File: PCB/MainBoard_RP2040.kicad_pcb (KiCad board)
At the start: 2 copper layers, 259.5 x 132.8 mm, 61 parts, among them J1 USB4105-GF-A, U1 ADC108S022CIMTX/NOPB, U10 DRV5053VAQDBZR, U11 DRV5053VAQDBZR, U12 DRV5053VAQDBZR, U13 DRV5053VAQDBZR, U14 DRV5053VAQDBZR, U15 DRV5053VAQDBZR, U16 DRV5053VAQDBZR, U17 DRV5053VAQDBZR, U18 DRV5053VAQDBZR, U19 DRV5053VAQDBZR, U20 ATmega32U4-A, U3 ADC108S022CIMTX/NOPB, U37 Pico, U4 DRV5053VAQDBZR, U5 DRV5053VAQDBZR, U6 DRV5053VAQDBZR, U7 DRV5053VAQDBZR, U8 DRV5053VAQDBZR, U9 DRV5053VAQDBZR, Y2 Crystal_GND24

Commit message: Removed other controller boards from RP2040
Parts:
- removed Brooks1: ~, BrooksBoards:BrooksP5Plus
- removed U36: ~, BrooksBoards:BrooksP5Mini
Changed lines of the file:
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@@
-		)
-	)
-	(footprint "BrooksBoards:BrooksP5Plus"
-		(layer "F.Cu")
-		(at 228.5 125 180)
-		(property "Reference" "Brooks1"
-			(at 0 -0.5 180)
-			(unlocked yes)
-			(layer "F.SilkS")
-			(effects
-				(font
-					(size 1 1)
-					(thickness 0.1)
-				)
-			)
-		)
-		(property "Value" "~"
-			(at 0 1 180)
-			(unlocked yes)
-			(layer "F.Fab")
-			(effects
-				(font
-					(size 1 1)
-					(thickness 0.15)
-				)
-			)
-		)
-		(property "Footprint" "BrooksBoards:BrooksP5Plus"
-			(at 0 0 180)
-			(unlocked yes)
-			(layer "F.Fab")
-			(hide yes)
-			(effects
-				(font
-					(size 1 1)
-					(thickness 0.15)
-				)
-			)
-		)
-		(property "Datasheet" ""
-			(at 0 0 180)
-			(unlocked yes)
-			(layer "F.Fab")
-			(hide yes)
-			(effects
-				(font
-					(size 1 1)
-					(thickness 0.15)
-				)
-			)
-		)
-		(property "Description" ""
-			(at 0 0 180)
-			(unlocked yes)
-			(layer "F.Fab")
-			(hide yes)
-			(effects
-				(font
-					(size 1 1)
-					(thickness 0.15)
-				)
-			)
-		)
-		(sheetname "Root")
-		(sheetfile "MainBoard.kicad_sch")
-		(attr through_hole)
-		(fp_rect
-			(start -48.2 -22.6)
-			(end 47.9 22.5)
-			(stroke
-				(width 0.1)
-				(type default)
-			)
-			(fill none)
-			(layer "F.SilkS")
-		)
-		(fp_text user "${REFERENCE}"
-			(at 0 2.5 180)
-			(unlocked yes)
-			(layer "F.Fab")
-			(effects
-				(font
-					(size 1 1)
-					(thickness 0.15)
-				)
-			)
 		)
 	)
@@
 				)
 			)
-		)
-	)
-	(footprint "BrooksBoards:BrooksP5Mini"
-		(layer "F.Cu")
-		(at 215.5 123.5)
-		(property "Reference" "U36"
-			(at 0 -0.5 0)
-			(unlocked yes)
-			(layer "F.SilkS")
-			(effects
-				(font
-					(size 1 1)
-					(thickness 0.1)
-				)
-			)
-		)
-		(property "Value" "~"
-			(at 0 1 0)
-			(unlocked yes)
-			(layer "F.Fab")
-			(effects
-				(font
-					(size 1 1)
-					(thickness 0.15)
-				)
-			)
-		)
-		(property "Footprint" "BrooksBoards:BrooksP5Mini"
-			(at 0 0 0)
-			(unlocked yes)
-			(layer "F.Fab")
-			(hide yes)
-			(effects
-				(font
-					(size 1 1)
-					(thickness 0.15)
-				)
-			)
-		)
-		(property "Datasheet" ""
-			(at 0 0 0)
-			(unlocked yes)
-			(layer "F.Fab")
-			(hide yes)
-			(effects
-				(font
-					(size 1 1)
-					(thickness 0.15)
-				)
-			)
-		)
-		(property "Description" ""
-			(at 0 0 0)
-			(unlocked yes)
-			(layer "F.Fab")
-			(hide yes)
-			(effects
-				(font
-					(size 1 1)
-					(thickness 0.15)
-				)
-			)
-		)
-		(sheetname "Root")
-		(sheetfile "MainBoard.kicad_sch")
-		(attr through_hole)
-		(fp_rect
-			(start -20 -20)
-			(end 20 20)
-			(stroke
-				(width 0.1)
-				(type default)
-			)
-			(fill none)
-			(layer "F.SilkS")
-		)
-		(fp_text user "${REFERENCE}"
-			(at 0 2.5 0)
-			(unlocked yes)
-			(layer "F.Fab")
-			(effects
-				(font
-					(size 1 1)
-					(thickness 0.15)
-				)
-			)

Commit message: Confirmed working, moving towards PCB v1.1
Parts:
- removed D1: LED_GREEN, LED_SMD:LED_0201_0603Metric
- removed R4: 1k, Resistor_SMD:R_0603_1608Metric
- added J2: Conn_01x06_Pin, Connector_PinHeader_2.54mm:PinHeader_2x03_P2.54mm_Vertical, F.Cu at (52.0, 71.5)
- added MB1: MagicBoots, Mayflash:MagicBoots, F.Cu at (175.0, 127.5)
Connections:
- net Net-(U20-~{RESET}) renamed /RST
- U37 pad 24: unconnected-(U37-GPIO18-Pad24) -> /HOST_D-
- U37 pad 25: unconnected-(U37-GPIO19-Pad25) -> /HOST_D+
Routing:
- net /HOST_D-: track 0.00 -> 148.7 mm
- net /HOST_D+: track 0.00 -> 143.7 mm
- net VCC: track 359.8 -> 454.2 mm, vias 6 -> 7
- net MOSI: track 153.0 -> 200.9 mm
- net MISO: track 152.7 -> 184.0 mm, vias 3 -> 4
- net SCLK: track 156.1 -> 173.6 mm, vias 3 -> 6
- net /RST: track 14.9 -> 25.8 mm
- net GND: track 109.8 -> 112.5 mm, vias 148 -> 191
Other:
- board size 259.5 x 132.8 mm -> 259.5 x 133 mm
- board text added: "Tristan Melton FaradayFightstick v1.1"
- board text removed: "MeltonTech"

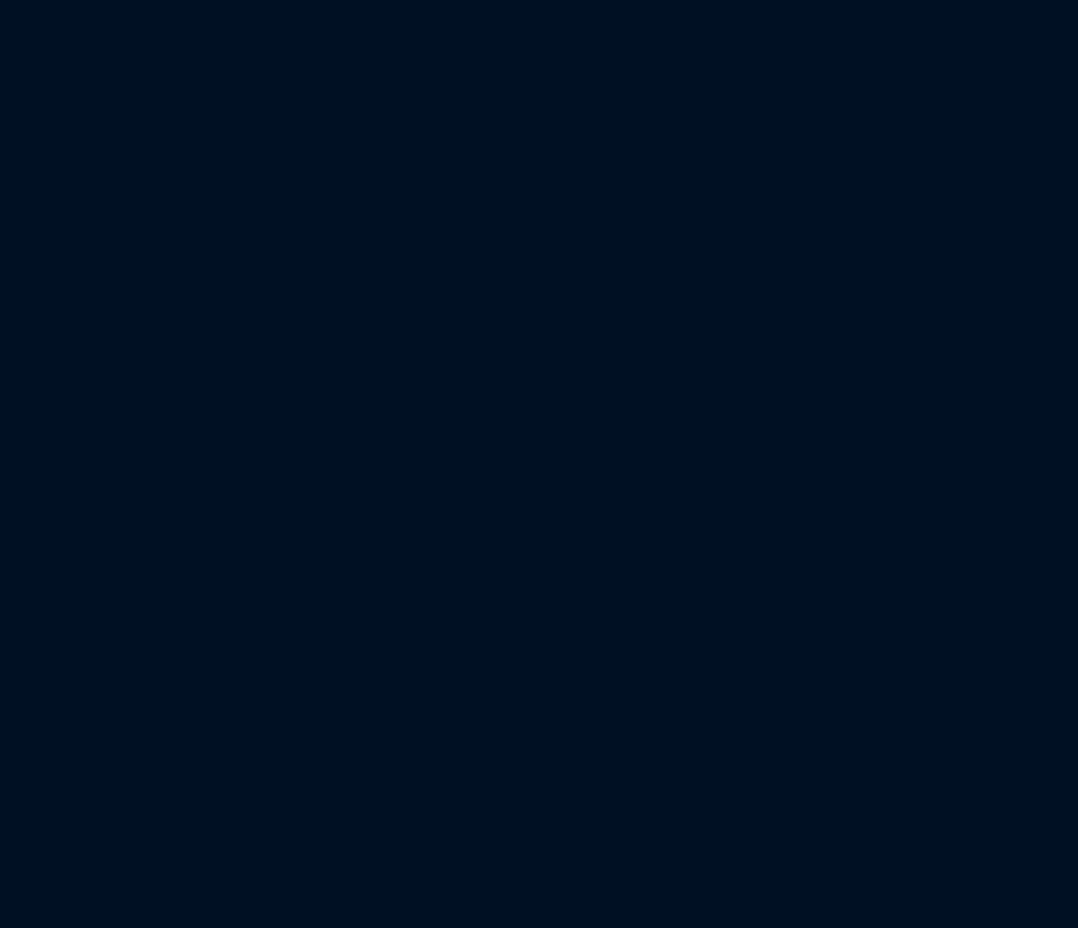
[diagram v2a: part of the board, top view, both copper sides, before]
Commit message: Added the additional components to support the ADCs
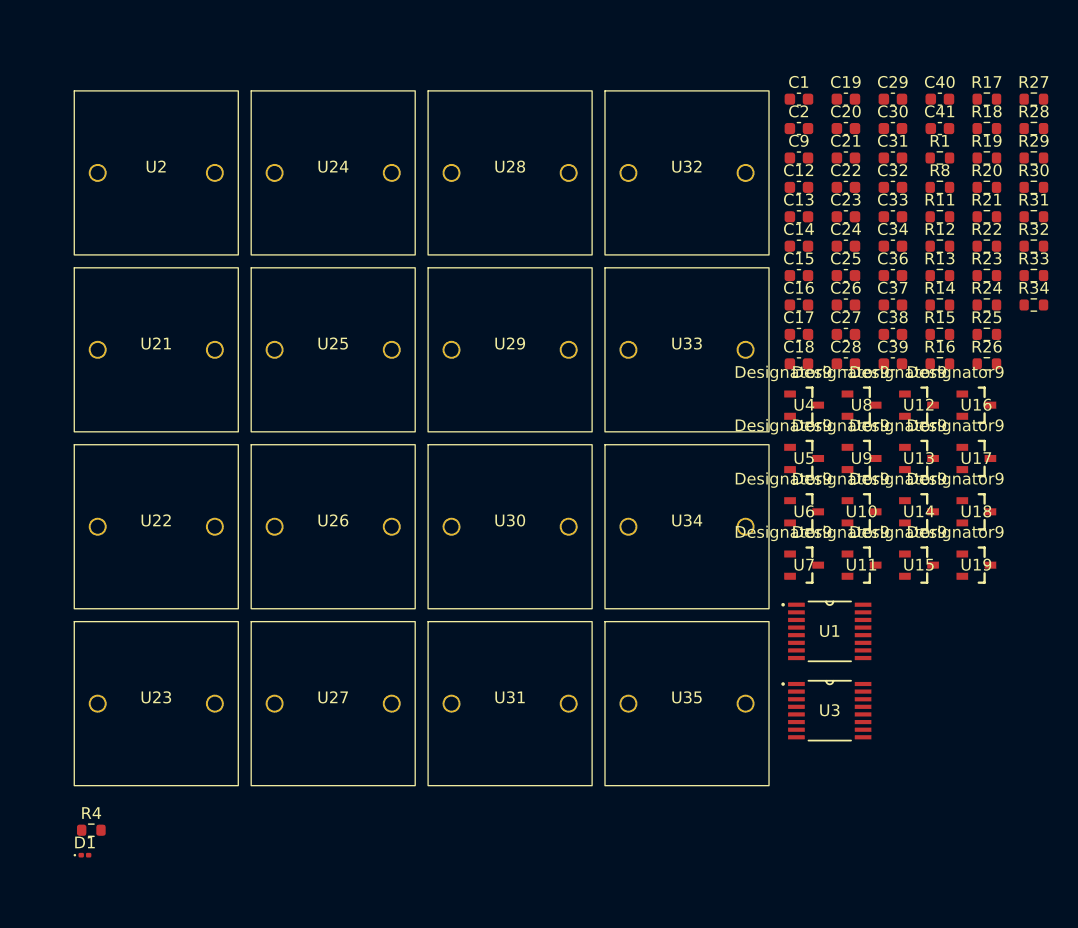
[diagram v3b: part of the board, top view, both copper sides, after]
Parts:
- added C1: 0.1u, Capacitor_SMD:C_0603_1608Metric, F.Cu at (384.0, 30.0)
- added C12: 1u, Capacitor_SMD:C_0603_1608Metric, F.Cu at (384.0, 37.6)
- added C13: 1n, Capacitor_SMD:C_0603_1608Metric, F.Cu at (384.0, 40.1)
- added C14: 1n, Capacitor_SMD:C_0603_1608Metric, F.Cu at (384.0, 42.6)
- added C15: 1n, Capacitor_SMD:C_0603_1608Metric, F.Cu at (384.0, 45.1)
- added C16: 1n, Capacitor_SMD:C_0603_1608Metric, F.Cu at (384.0, 47.6)
- added C17: 1n, Capacitor_SMD:C_0603_1608Metric, F.Cu at (384.0, 50.1)
- added C18: 1n, Capacitor_SMD:C_0603_1608Metric, F.Cu at (384.0, 52.6)
- added C19: 0.1u, Capacitor_SMD:C_0603_1608Metric, F.Cu at (388.0, 30.0)
- added C2: 1u, Capacitor_SMD:C_0603_1608Metric, F.Cu at (384.0, 32.5)
- added C20: 1u, Capacitor_SMD:C_0603_1608Metric, F.Cu at (388.0, 32.5)
- added C21: 1n, Capacitor_SMD:C_0603_1608Metric, F.Cu at (388.0, 35.1)
- added C22: 1n, Capacitor_SMD:C_0603_1608Metric, F.Cu at (388.0, 37.6)
- added C23: 1n, Capacitor_SMD:C_0603_1608Metric, F.Cu at (388.0, 40.1)
- added C24: 1n, Capacitor_SMD:C_0603_1608Metric, F.Cu at (388.0, 42.6)
- added C25: 1n, Capacitor_SMD:C_0603_1608Metric, F.Cu at (388.0, 45.1)
- added C26: 1n, Capacitor_SMD:C_0603_1608Metric, F.Cu at (388.0, 47.6)
- added C27: 1n, Capacitor_SMD:C_0603_1608Metric, F.Cu at (388.0, 50.1)
- added C28: 1n, Capacitor_SMD:C_0603_1608Metric, F.Cu at (388.0, 52.6)
- added C29: 1n, Capacitor_SMD:C_0603_1608Metric, F.Cu at (392.0, 30.0)
- added C30: 1n, Capacitor_SMD:C_0603_1608Metric, F.Cu at (392.0, 32.5)
- added C31: 1n, Capacitor_SMD:C_0603_1608Metric, F.Cu at (392.0, 35.1)
- added C32: 1n, Capacitor_SMD:C_0603_1608Metric, F.Cu at (392.0, 37.6)
- added C33: 0.1u, Capacitor_SMD:C_0603_1608Metric, F.Cu at (392.0, 40.1)
- added C34: 1u, Capacitor_SMD:C_0603_1608Metric, F.Cu at (392.0, 42.6)
- added C36: 1n, Capacitor_SMD:C_0603_1608Metric, F.Cu at (392.0, 45.1)
- added C37: 1n, Capacitor_SMD:C_0603_1608Metric, F.Cu at (392.0, 47.6)
- added C38: 1n, Capacitor_SMD:C_0603_1608Metric, F.Cu at (392.0, 50.1)
- added C39: 1n, Capacitor_SMD:C_0603_1608Metric, F.Cu at (392.0, 52.6)
- added C40: 1n, Capacitor_SMD:C_0603_1608Metric, F.Cu at (396.1, 30.0)
- added C41: 1n, Capacitor_SMD:C_0603_1608Metric, F.Cu at (396.1, 32.5)
- added C9: 0.1u, Capacitor_SMD:C_0603_1608Metric, F.Cu at (384.0, 35.1)
- added D1: LED_GREEN, LED_SMD:LED_0201_0603Metric, F.Cu at (323.1, 94.6)
- added R1: 22, Resistor_SMD:R_0603_1608Metric, F.Cu at (396.1, 35.1)
- added R11: 22, Resistor_SMD:R_0603_1608Metric, F.Cu at (396.1, 40.1)
- added R12: 22, Resistor_SMD:R_0603_1608Metric, F.Cu at (396.1, 42.6)
- added R13: 22, Resistor_SMD:R_0603_1608Metric, F.Cu at (396.1, 45.1)
- added R14: 22, Resistor_SMD:R_0603_1608Metric, F.Cu at (396.1, 47.6)
- added R15: 22, Resistor_SMD:R_0603_1608Metric, F.Cu at (396.1, 50.1)
- added R16: 22, Resistor_SMD:R_0603_1608Metric, F.Cu at (396.1, 52.6)
- added R17: 22, Resistor_SMD:R_0603_1608Metric, F.Cu at (400.1, 30.0)
- added R18: 22, Resistor_SMD:R_0603_1608Metric, F.Cu at (400.1, 32.5)
- added R19: 22, Resistor_SMD:R_0603_1608Metric, F.Cu at (400.1, 35.1)
- added R20: 22, Resistor_SMD:R_0603_1608Metric, F.Cu at (400.1, 37.6)
- added R21: 22, Resistor_SMD:R_0603_1608Metric, F.Cu at (400.1, 40.1)
- added R22: 22, Resistor_SMD:R_0603_1608Metric, F.Cu at (400.1, 42.6)
- added R23: 22, Resistor_SMD:R_0603_1608Metric, F.Cu at (400.1, 45.1)
- added R24: 22, Resistor_SMD:R_0603_1608Metric, F.Cu at (400.1, 47.6)
- added R25: 22, Resistor_SMD:R_0603_1608Metric, F.Cu at (400.1, 50.1)
- added R26: 22, Resistor_SMD:R_0603_1608Metric, F.Cu at (400.1, 52.6)
- added R27: 51, Resistor_SMD:R_0603_1608Metric, F.Cu at (404.1, 30.0)
- added R28: 22, Resistor_SMD:R_0603_1608Metric, F.Cu at (404.1, 32.5)
- added R29: 22, Resistor_SMD:R_0603_1608Metric, F.Cu at (404.1, 35.1)
- added R30: 22, Resistor_SMD:R_0603_1608Metric, F.Cu at (404.1, 37.6)
- added R31: 22, Resistor_SMD:R_0603_1608Metric, F.Cu at (404.1, 40.1)
- added R32: 22, Resistor_SMD:R_0603_1608Metric, F.Cu at (404.1, 42.6)
- added R33: 22, Resistor_SMD:R_0603_1608Metric, F.Cu at (404.1, 45.1)
- added R34: 51, Resistor_SMD:R_0603_1608Metric, F.Cu at (404.1, 47.6)
- added R4: 1k, Resistor_SMD:R_0603_1608Metric, F.Cu at (323.6, 92.4)
- added R8: 22, Resistor_SMD:R_0603_1608Metric, F.Cu at (396.1, 37.6)
- added U1: ADC108S022CIMTX/NOPB, ADCs:MTC16, F.Cu at (386.7, 75.5)
- added U10: DRV5053VAQDBZR, HallEffect:DBZ0003A_N, F.Cu at (389.4, 65.3)
- added U11: DRV5053VAQDBZR, HallEffect:DBZ0003A_N, F.Cu at (389.4, 69.8)
- added U12: DRV5053VAQDBZR, HallEffect:DBZ0003A_N, F.Cu at (394.3, 56.2)
- added U13: DRV5053VAQDBZR, HallEffect:DBZ0003A_N, F.Cu at (394.3, 60.7)
- added U14: DRV5053VAQDBZR, HallEffect:DBZ0003A_N, F.Cu at (394.3, 65.3)
- added U15: DRV5053VAQDBZR, HallEffect:DBZ0003A_N, F.Cu at (394.3, 69.8)
- added U16: DRV5053VAQDBZR, HallEffect:DBZ0003A_N, F.Cu at (399.2, 56.2)
- added U17: DRV5053VAQDBZR, HallEffect:DBZ0003A_N, F.Cu at (399.2, 60.7)
- added U18: DRV5053VAQDBZR, HallEffect:DBZ0003A_N, F.Cu at (399.2, 65.3)
- added U19: DRV5053VAQDBZR, HallEffect:DBZ0003A_N, F.Cu at (399.2, 69.8)
- added U2: ~, key-switches:Gateron Jade Pro Magnetic, F.Cu at (329.2, 36.3)
- added U21: ~, key-switches:Gateron Jade Pro Magnetic, F.Cu at (329.2, 51.4)
- added U22: ~, key-switches:Gateron Jade Pro Magnetic, F.Cu at (329.2, 66.5)
- added U23: ~, key-switches:Gateron Jade Pro Magnetic, F.Cu at (329.2, 81.6)
- added U24: ~, key-switches:Gateron Jade Pro Magnetic, F.Cu at (344.3, 36.3)
- added U25: ~, key-switches:Gateron Jade Pro Magnetic, F.Cu at (344.3, 51.4)
- added U26: ~, key-switches:Gateron Jade Pro Magnetic, F.Cu at (344.3, 66.5)
- added U27: ~, key-switches:Gateron Jade Pro Magnetic, F.Cu at (344.3, 81.6)
- added U28: ~, key-switches:Gateron Jade Pro Magnetic, F.Cu at (359.4, 36.3)
- added U29: ~, key-switches:Gateron Jade Pro Magnetic, F.Cu at (359.4, 51.4)
- added U3: ADC108S022CIMTX/NOPB, ADCs:MTC16, F.Cu at (386.7, 82.2)
- added U30: ~, key-switches:Gateron Jade Pro Magnetic, F.Cu at (359.4, 66.5)
- added U31: ~, key-switches:Gateron Jade Pro Magnetic, F.Cu at (359.4, 81.6)
- added U32: ~, key-switches:Gateron Jade Pro Magnetic, F.Cu at (374.5, 36.3)
- added U33: ~, key-switches:Gateron Jade Pro Magnetic, F.Cu at (374.5, 51.4)
- added U34: ~, key-switches:Gateron Jade Pro Magnetic, F.Cu at (374.5, 66.5)
- added U35: ~, key-switches:Gateron Jade Pro Magnetic, F.Cu at (374.5, 81.6)
- added U4: DRV5053VAQDBZR, HallEffect:DBZ0003A_N, F.Cu at (384.5, 56.2)
- added U5: DRV5053VAQDBZR, HallEffect:DBZ0003A_N, F.Cu at (384.5, 60.7)
- added U6: DRV5053VAQDBZR, HallEffect:DBZ0003A_N, F.Cu at (384.5, 65.3)
- added U7: DRV5053VAQDBZR, HallEffect:DBZ0003A_N, F.Cu at (384.5, 69.8)
- added U8: DRV5053VAQDBZR, HallEffect:DBZ0003A_N, F.Cu at (389.4, 56.2)
- added U9: DRV5053VAQDBZR, HallEffect:DBZ0003A_N, F.Cu at (389.4, 60.7)

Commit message: Working on layout of PCB to include the other components....
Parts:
- moved U2 2.90 mm to (328.5, 33.5)
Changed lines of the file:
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@@
 	(footprint "key-switches:Gateron Jade Pro Magnetic"
 		(layer "F.Cu")
-		(at 329.1702 36.326301)
+		(at 328.5 33.5)
 		(property "Reference" "U2"
 			(at 0 -0.5 0)
@@
 			(polygon
 				(pts
-					(xy 323.1702 42.326301) (xy 335.1702 42.326301) (xy 335.1702 30.326301) (xy 323.1702 30.326301)
+					(xy 322.5 39.5) (xy 334.5 39.5) (xy 334.5 27.5) (xy 322.5 27.5)
 				)
 			)

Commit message: PCB Updated to include the ADC improved components
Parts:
- removed C13, C21, C22, C23, C27, C28, C29, C36: 1n, Capacitor_SMD:C_0603_1608Metric
- removed D1: LED_GREEN, LED_SMD:LED_0201_0603Metric
- removed R1, R15, R16, R17, R21, R22, R23, R28: 22, Resistor_SMD:R_0603_1608Metric
- removed R4: 1k, Resistor_SMD:R_0603_1608Metric
- removed the U1 at (182.8, 68.0)
- removed the U10 at (103.2, 63.0)
- removed the U11 at (140.2, 66.0)
- removed the U12 at (141.2, 102.0)
- removed the U13 at (171.5, 88.5)
- removed the U14 at (236.0, 72.0)
- removed the U15 at (156.7, 30.0)
- removed the U16 at (94.0, 30.0)
- removed the U17 at (115.0, 37.0)
- removed the U18 at (136.3, 37.1)
- removed the U19 at (202.7, 79.0)
- removed the U2 at (41.7, 40.1)
- removed the U21 at (94.0, 30.0)
- removed the U22 at (115.0, 37.0)
- removed the U23 at (156.7, 30.0)
- removed the U24 at (72.9, 49.5)
- removed the U25 at (235.0, 36.0)
- removed the U26 at (236.0, 72.0)
- removed the U27 at (136.3, 37.1)
- removed the U28 at (103.2, 63.0)
- removed the U29 at (170.5, 52.5)
- removed the U3 at (77.0, 82.5)
- removed the U30 at (202.7, 79.0)
- removed the U31 at (201.7, 43.1)
- removed the U32 at (140.2, 66.0)
- removed the U33 at (117.7, 130.0)
- removed the U34 at (141.2, 101.9)
- removed the U35 at (171.5, 88.5)
- removed the U4 at (170.5, 52.5)
- removed the U5 at (201.7, 43.1)
- removed the U6 at (235.0, 36.0)
- removed the U7 at (117.7, 130.0)
- removed the U8 at (72.9, 49.5)
- removed the U9 at (41.7, 40.1)
- C1, C12, C14, C15, C16, C17, C18, C19, C2, C20, C24, C25, C26, C30, C31, C32, C33, C34, C37, C38, C39, C41, C9, R11, R12, R13, R14, R18, R19, R20, R24, R25, R26, R27, R29, R30, R31, R33, R34, R8, U1, U10, U11, U12, U13, U14, U15, U16, U17, U18, U19, U3, U4, U5, U6, U7, U8, U9: moved to B.Cu
- moved U9 348.3 mm to (41.7, 40.0), turned to 180 degrees
- moved R34 333.5 mm to (72.5, 83.5)
- moved R29 331.9 mm to (74.5, 74.5)
- moved R30 328.6 mm to (77.5, 74.0), turned to -90 degrees
- moved R31 326.3 mm to (79.5, 74.0), turned to -90 degrees
- moved R32 324.8 mm to (81.2, 78.0), turned to 180 degrees
- moved C34 324.4 mm to (69.5, 77.5), turned to -90 degrees
- moved C33 323.3 mm to (71.0, 78.3), turned to -90 degrees
- moved R33 323.1 mm to (82.5, 76.5), turned to 180 degrees
- moved R26 322.8 mm to (79.5, 90.5), turned to 90 degrees
- moved R25 319.5 mm to (82.0, 80.5), turned to 180 degrees
- moved R24 319.1 mm to (83.5, 87.5), turned to 180 degrees
- moved C37 318.8 mm to (74.5, 76.0)
- moved C40 318.4 mm to (81.5, 79.5), turned to 180 degrees
- moved C2 318.3 mm to (70.0, 84.3), turned to -90 degrees
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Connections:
- U1 pad 1: Net-(U1-~CS) -> NOT_CS1
- U1 pad 14: Net-(U1-DIN) -> MOSI
- U1 pad 15: Net-(U1-DOUT) -> MISO
- U1 pad 16: Net-(U1-SCLK) -> SCLK
- U3 pad 1: Net-(U3-~CS) -> NOT_CS2
- U3 pad 14: Net-(U3-DIN) -> MOSI
- U3 pad 15: Net-(U3-DOUT) -> MISO
- U3 pad 16: Net-(U3-SCLK) -> SCLK
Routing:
- net Net-(U3-VD): track 0.00 -> 10.4 mm
- net Net-(U1-VD): track 0.00 -> 8.55 mm
- net TURBOA: track 87.3 -> 78.8 mm, vias 4 -> 2
- net Net-(U1-IN1): track 0.00 -> 8.44 mm
- net Net-(U1-IN6): track 0.00 -> 8.39 mm
- net Net-(U3-IN7): track 0.00 -> 8.36 mm, vias 0 -> 2
- net MKA: track 26.0 -> 18.0 mm
- net Net-(U3-IN6): track 0.00 -> 7.84 mm
- net SHKA: track 56.8 -> 49.1 mm
- net Net-(U3-IN1): track 0.00 -> 7.57 mm
- net Net-(U3-IN0): track 0.00 -> 7.24 mm
- net Net-(U1-IN4): track 0.00 -> 7.04 mm
- net Net-(U3-IN3): track 0.00 -> 7.03 mm, vias 0 -> 1
- net Net-(U3-IN2): track 0.00 -> 6.98 mm
- net SELECTA: track 108.7 -> 101.8 mm, vias 4 -> 3
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
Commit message: Added protective diodes to RP2040 Board
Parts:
- added D3: D, Diode_SMD:D_0603_1608Metric, B.Cu at (31.2, 102.0)
- added D4: D, Diode_SMD:D_0603_1608Metric, B.Cu at (29.8, 93.0)
- added D5: D, Diode_SMD:D_0603_1608Metric, B.Cu at (265.8, 91.0)
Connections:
- J1 pad A4_B9: VCC -> Net-(D3-A)
- J1 pad B4_A9: VCC -> Net-(D3-A)
- U37 pad 40: VCC -> Net-(D5-A)
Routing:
- net Net-(D3-A): track 0.00 -> 13.3 mm
- net Net-(D5-A): track 0.00 -> 6.76 mm
- net VCC: track 451.5 -> 446.1 mm, vias 7 -> 9
